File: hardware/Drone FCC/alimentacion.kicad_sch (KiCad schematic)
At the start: 1 part, among them J28 Conn_01x06

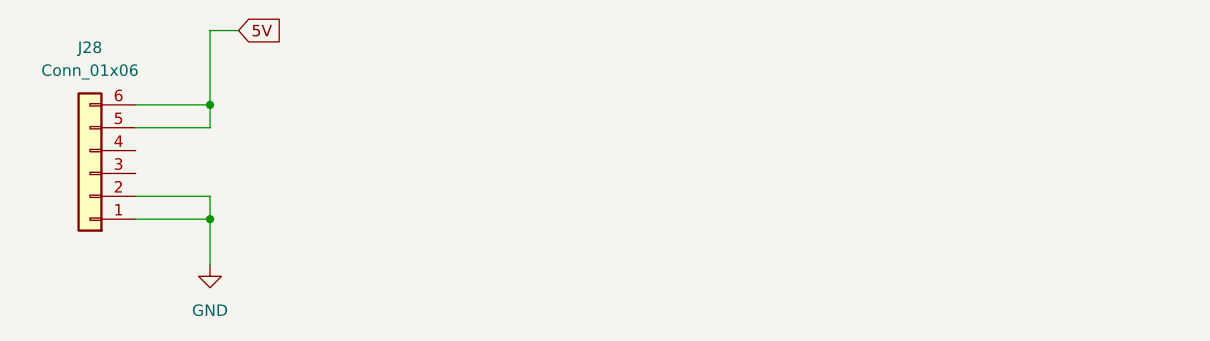
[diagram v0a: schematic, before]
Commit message: add LDO 3V3 to schematic
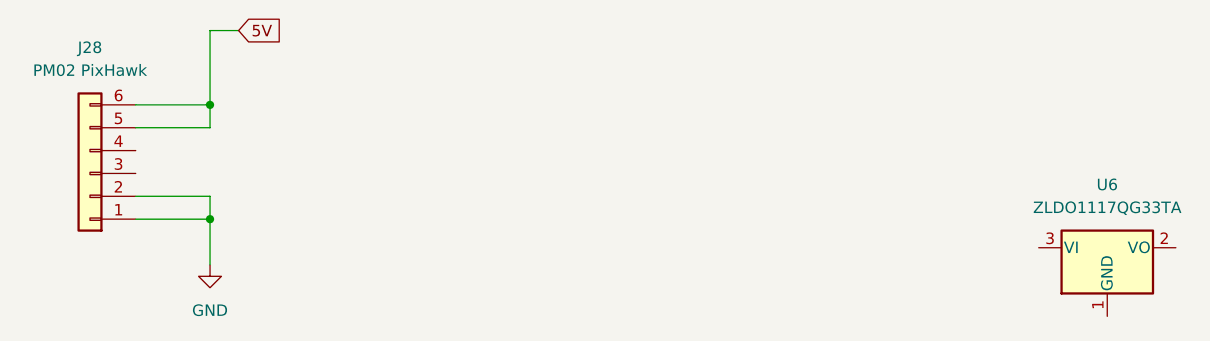
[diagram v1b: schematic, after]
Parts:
- added U6: ZLDO1117QG33TA, Package_TO_SOT_SMD:SOT-223-3_TabPin2, symbol Regulator_Linear:NCP1117-3.3_SOT223
- J28: value Conn_01x06 -> PM02 PixHawk
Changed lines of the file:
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@@
     (in_bom yes) (on_board yes) (fields_autoplaced)
     (property "Reference" "J28" (id 0) (at 41.275 35.56 0))
-    (property "Value" "Conn_01x06" (id 1) (at 41.275 38.1 0))
+    (property "Value" "PM02 PixHawk" (id 1) (at 41.275 38.1 0))
     (property "Footprint" "Connector_Hirose:Hirose_DF13C_CL535-0406-3-51_1x06-1MP_P1.25mm_Vertical" (id 2) (at 41.275 49.53 0)
       (effects (font (size 1.27 1.27)) hide)
@@
     (pin "6")
   )
+  (symbol (lib_id "Regulator_Linear:NCP1117-3.3_SOT223") (at 154.305 57.785 0) (unit 1)
+    (in_bom yes) (on_board yes) (fields_autoplaced)
+    (property "Reference" "U6" (id 0) (at 154.305 50.8 0))
+    (property "Value" "ZLDO1117QG33TA" (id 1) (at 154.305 53.34 0))
+    (property "Footprint" "Package_TO_SOT_SMD:SOT-223-3_TabPin2" (id 2) (at 154.305 52.705 0)
+      (effects (font (size 1.27 1.27)) hide)
+    )
+    (property "Datasheet" "http://www.onsemi.com/pub_link/Collateral/NCP1117-D.PDF" (id 3) (at 156.845 64.135 0)
+      (effects (font (size 1.27 1.27)) hide)
+    )
+    (pin "1")
+    (pin "2")
+    (pin "3")
+  )
   (symbol (lib_id "power:GND") (at 54.61 59.69 0) (unit 1)

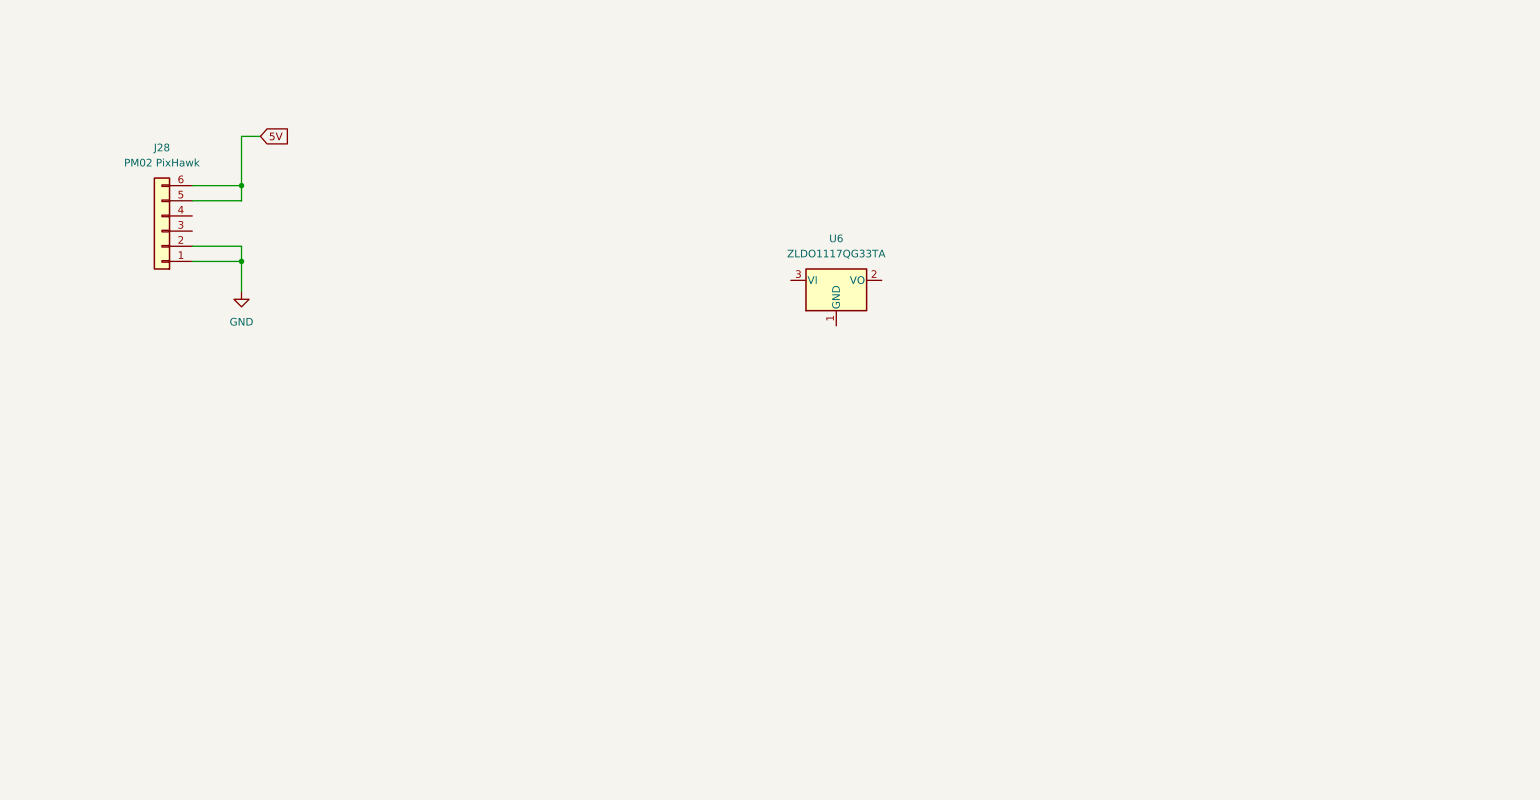
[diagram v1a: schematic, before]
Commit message: add soft-start for USB connector
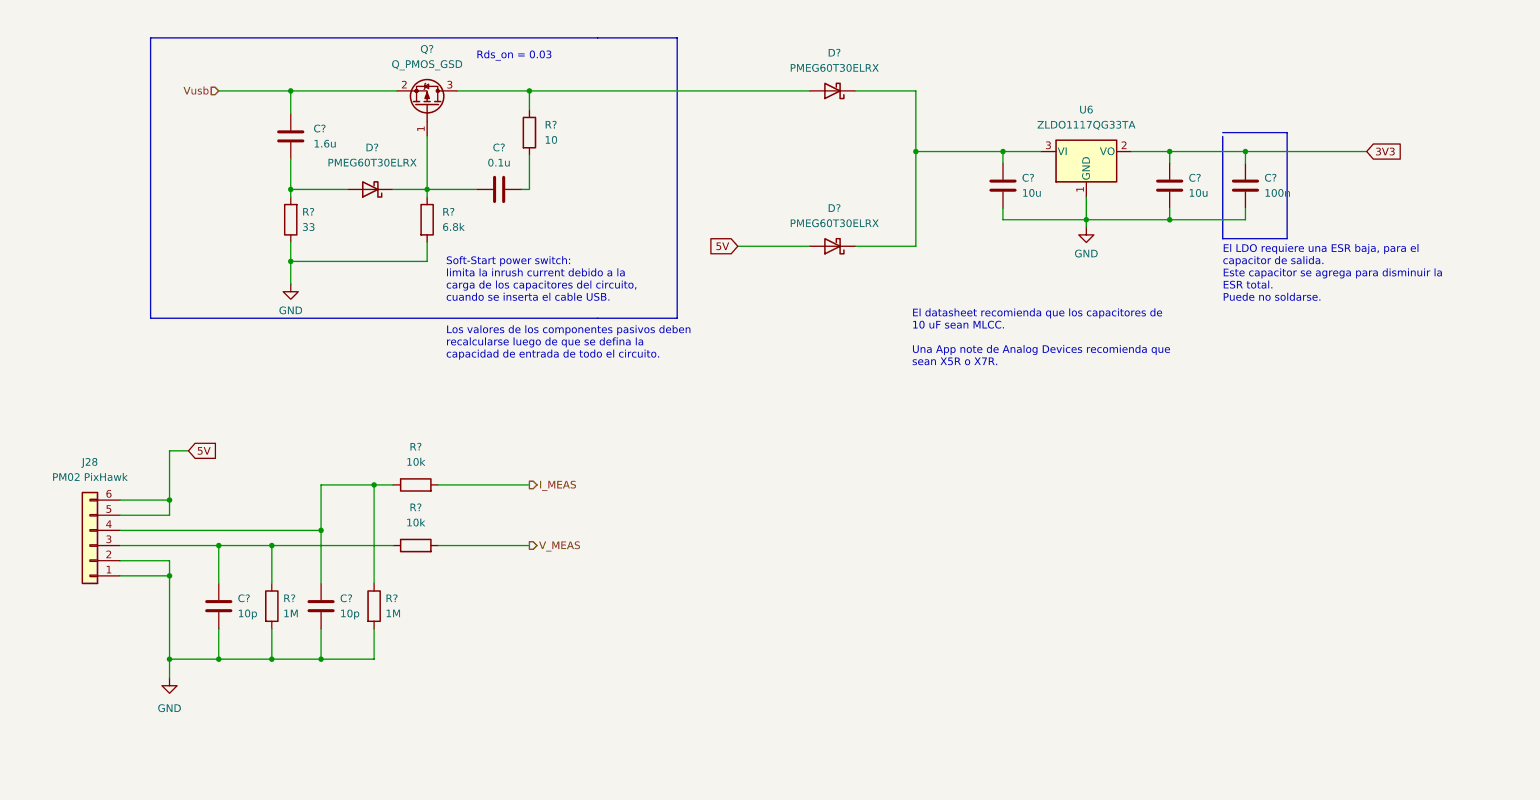
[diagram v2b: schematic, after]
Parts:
- added C?: 0.1u, symbol Device:C
- added C? (x2): 10u, symbol Device:C
- added C?: 1.6u, symbol Device:C
- added C? (x2): 10p, symbol Device:C
- added C?: 100n, symbol Device:C
- added D? (x3): PMEG60T30ELRX, symbol Device:D_Schottky
- added Q?: Q_PMOS_GSD, symbol Device:Q_PMOS_GSD
- added R?: 6.8k, symbol Device:R
- added R? (x2): 10k, symbol Device:R
- added R? (x2): 1M, symbol Device:R
- added R?: 10, symbol Device:R
- added R?: 33, symbol Device:R
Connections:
- net 5V: now also D?.2 (A)
- net GND: now also U6.1 (GND), C?.2, C?.2, C?.2, C?.2, C?.2, R?.1, R?.2, R?.2, R?.2
- net at J28.3 (Pin_3): now also C?.1, R?.1, R?.1
- net at J28.4 (Pin_4): now also C?.1, R?.1, R?.1
- net 3V3: now reaches U6.2 (VO)
- net 3V3: now also C?.1, C?.1
- net at U6.3 (VI): now also C?.1, D?.1 (K), D?.1 (K)
- new net: C?.1, D?.1 (K), Q?.1 (G), R?.1
- new net: C?.2, R?.2
- new net: D?.2 (A), Q?.3 (D), R?.1
- new net: C?.2, D?.2 (A), R?.2
- new net I_MEAS: R?.2
- new net V_MEAS: R?.2
- new net Vusb: C?.1, Q?.2 (S)
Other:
- note added: "El LDO requiere una ESR baja, para el capacitor de salida. Este capacitor se agrega para disminuir la ESR total. Puede no soldarse."
- note added: "El datasheet recomienda que los capacitores de 10 uF sean MLCC. Una App note de Analog Devices recomienda que sean X5R o X7R."
- note added: "Los valores de los componentes pasivos deben recalcularse luego de que se defina la capacidad de entrada de todo el circuito."
- note added: "Rds_on = 0.03"
- note added: "Soft-Start power switch: limita la inrush current debido a la carga de los capacitores del circuito, cuando se inserta el cable USB."
- moved on the sheet: J28, U6

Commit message: add CAN schematic
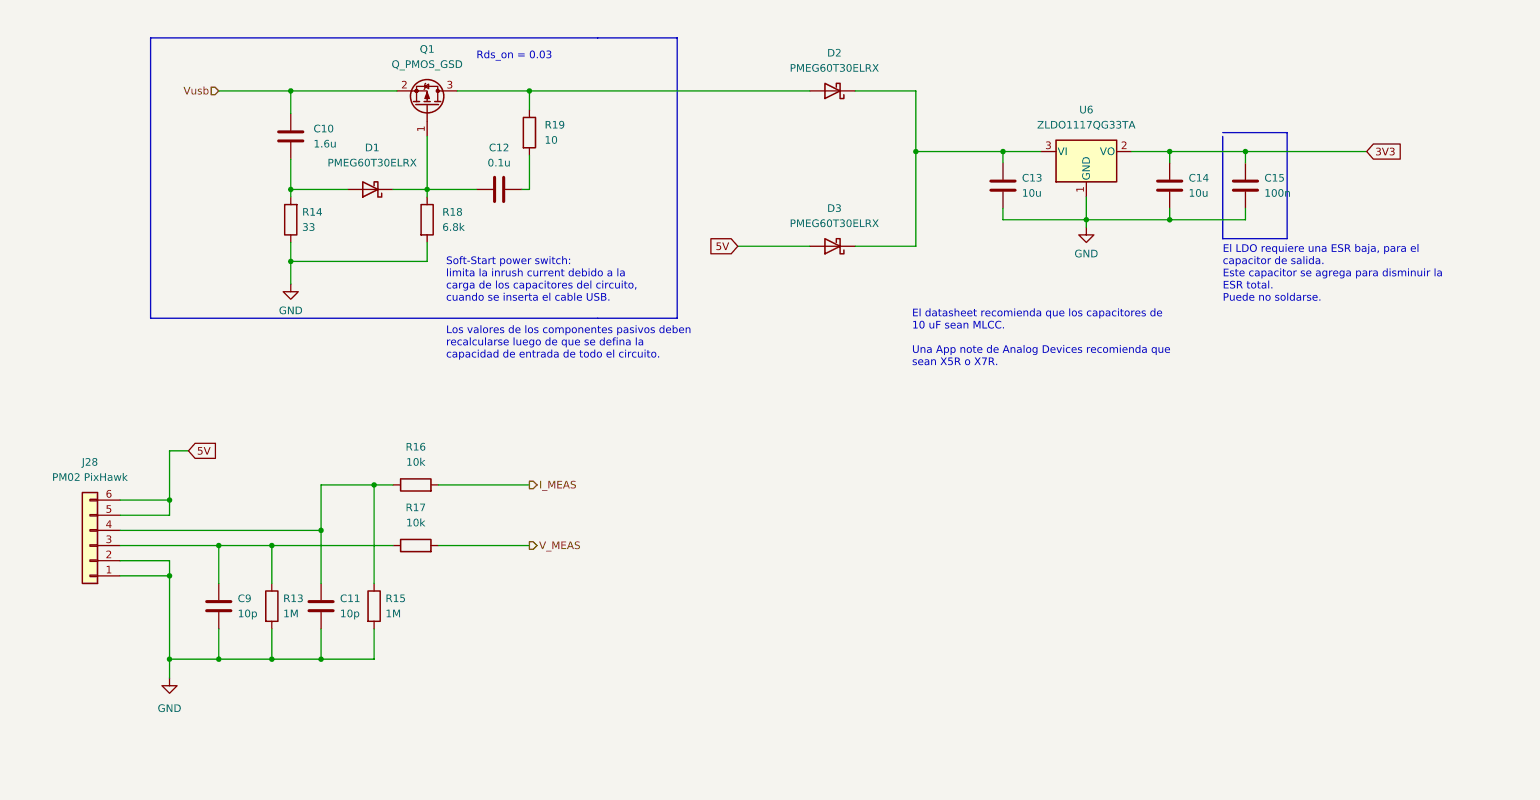
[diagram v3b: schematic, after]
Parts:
- gave numbers to parts that had none: 18
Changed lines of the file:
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@@
   (symbol (lib_id "Device:C") (at 97.79 42.545 90) (unit 1)
     (in_bom yes) (on_board yes) (fields_autoplaced)
-    (property "Reference" "C?" (id 0) (at 97.79 35.56 90))
+    (property "Reference" "C12" (id 0) (at 97.79 35.56 90))
     (property "Value" "0.1u" (id 1) (at 97.79 38.1 90))
     (property "Footprint" "" (id 2) (at 101.6 41.5798 0)
@@
   (symbol (lib_id "Device:Q_PMOS_GSD") (at 85.725 28.575 270) (mirror x) (unit 1)
     (in_bom yes) (on_board yes) (fields_autoplaced)
-    (property "Reference" "Q?" (id 0) (at 85.725 19.05 90))
+    (property "Reference" "Q1" (id 0) (at 85.725 19.05 90))
     (property "Value" "Q_PMOS_GSD" (id 1) (at 85.725 21.59 90))
     (property "Footprint" "" (id 2) (at 88.265 23.495 0)
@@
   (symbol (lib_id "Device:D_Schottky") (at 76.2 42.545 180) (unit 1)
     (in_bom yes) (on_board yes) (fields_autoplaced)
-    (property "Reference" "D?" (id 0) (at 76.5175 35.56 0))
+    (property "Reference" "D1" (id 0) (at 76.5175 35.56 0))
     (property "Value" "PMEG60T30ELRX " (id 1) (at 76.5175 38.1 0))
     (property "Footprint" "" (id 2) (at 76.2 42.545 0)
@@
   (symbol (lib_id "Device:R") (at 85.725 47.625 0) (unit 1)
     (in_bom yes) (on_board yes) (fields_autoplaced)
-    (property "Reference" "R?" (id 0) (at 88.265 46.3549 0)
+    (property "Reference" "R18" (id 0) (at 88.265 46.3549 0)
       (effects (font (size 1.27 1.27)) (justify left))
     )
@@
   (symbol (lib_id "Device:R") (at 83.82 102.235 90) (unit 1)
     (in_bom yes) (on_board yes) (fields_autoplaced)
-    (property "Reference" "R?" (id 0) (at 83.82 95.885 90))
+    (property "Reference" "R17" (id 0) (at 83.82 95.885 90))
     (property "Value" "10k" (id 1) (at 83.82 98.425 90))
     (property "Footprint" "" (id 2) (at 83.82 104.013 90)
@@
   (symbol (lib_id "power:GND") (at 62.865 58.42 0) (unit 1)
     (in_bom yes) (on_board yes) (fields_autoplaced)
-    (property "Reference" "#PWR?" (id 0) (at 62.865 64.77 0)
+    (property "Reference" "#PWR0128" (id 0) (at 62.865 64.77 0)
       (effects (font (size 1.27 1.27)) hide)
     )
@@
   (symbol (lib_id "Device:R") (at 76.835 112.395 0) (unit 1)
     (in_bom yes) (on_board yes) (fields_autoplaced)
-    (property "Reference" "R?" (id 0) (at 78.74 111.1249 0)
+    (property "Reference" "R15" (id 0) (at 78.74 111.1249 0)
       (effects (font (size 1.27 1.27)) (justify left))
     )
@@
   (symbol (lib_id "Device:C") (at 182.245 41.91 0) (unit 1)
     (in_bom yes) (on_board yes) (fields_autoplaced)
-    (property "Reference" "C?" (id 0) (at 185.42 40.6399 0)
+    (property "Reference" "C13" (id 0) (at 185.42 40.6399 0)
       (effects (font (size 1.27 1.27)) (justify left))
     )
@@
   (symbol (lib_id "Device:R") (at 59.69 112.395 0) (unit 1)
     (in_bom yes) (on_board yes) (fields_autoplaced)
-    (property "Reference" "R?" (id 0) (at 61.595 111.1249 0)
+    (property "Reference" "R13" (id 0) (at 61.595 111.1249 0)
       (effects (font (size 1.27 1.27)) (justify left))
     )
@@
   (symbol (lib_id "Device:C") (at 62.865 33.655 0) (unit 1)
     (in_bom yes) (on_board yes) (fields_autoplaced)
-    (property "Reference" "C?" (id 0) (at 66.675 32.3849 0)
+    (property "Reference" "C10" (id 0) (at 66.675 32.3849 0)
       (effects (font (size 1.27 1.27)) (justify left))
     )
@@
   (symbol (lib_id "Device:R") (at 102.87 33.02 0) (unit 1)
     (in_bom yes) (on_board yes) (fields_autoplaced)
-    (property "Reference" "R?" (id 0) (at 105.41 31.7499 0)
+    (property "Reference" "R19" (id 0) (at 105.41 31.7499 0)
       (effects (font (size 1.27 1.27)) (justify left))
     )
@@
   (symbol (lib_id "Device:C") (at 50.8 112.395 0) (unit 1)
     (in_bom yes) (on_board yes) (fields_autoplaced)
-    (property "Reference" "C?" (id 0) (at 53.975 111.1249 0)
+    (property "Reference" "C9" (id 0) (at 53.975 111.1249 0)
       (effects (font (size 1.27 1.27)) (justify left))
     )
@@
   (symbol (lib_id "Device:R") (at 62.865 47.625 180) (unit 1)
     (in_bom yes) (on_board yes) (fields_autoplaced)
-    (property "Reference" "R?" (id 0) (at 64.77 46.3549 0)
+    (property "Reference" "R14" (id 0) (at 64.77 46.3549 0)
       (effects (font (size 1.27 1.27)) (justify right))
     )
@@
   (symbol (lib_id "Device:D_Schottky") (at 153.67 26.035 180) (unit 1)
     (in_bom yes) (on_board yes) (fields_autoplaced)
-    (property "Reference" "D?" (id 0) (at 153.9875 19.685 0))
+    (property "Reference" "D2" (id 0) (at 153.9875 19.685 0))
     (property "Value" "PMEG60T30ELRX " (id 1) (at 153.9875 22.225 0))
     (property "Footprint" "" (id 2) (at 153.67 26.035 0)
@@
   (symbol (lib_id "Device:C") (at 222.885 41.91 0) (unit 1)
     (in_bom yes) (on_board yes) (fields_autoplaced)
-    (property "Reference" "C?" (id 0) (at 226.06 40.6399 0)
+    (property "Reference" "C15" (id 0) (at 226.06 40.6399 0)
       (effects (font (size 1.27 1.27)) (justify left))
     )
@@
   (symbol (lib_id "Device:R") (at 83.82 92.075 90) (unit 1)
     (in_bom yes) (on_board yes) (fields_autoplaced)
-    (property "Reference" "R?" (id 0) (at 83.82 85.725 90))
+    (property "Reference" "R16" (id 0) (at 83.82 85.725 90))
     (property "Value" "10k" (id 1) (at 83.82 88.265 90))
     (property "Footprint" "" (id 2) (at 83.82 93.853 90)
@@
   (symbol (lib_id "Device:C") (at 210.185 41.91 0) (unit 1)
     (in_bom yes) (on_board yes) (fields_autoplaced)
-    (property "Reference" "C?" (id 0) (at 213.36 40.6399 0)
+    (property "Reference" "C14" (id 0) (at 213.36 40.6399 0)
       (effects (font (size 1.27 1.27)) (justify left))
     )
@@
   (symbol (lib_id "Device:C") (at 67.945 112.395 0) (unit 1)
     (in_bom yes) (on_board yes) (fields_autoplaced)
-    (property "Reference" "C?" (id 0) (at 71.12 111.1249 0)
+    (property "Reference" "C11" (id 0) (at 71.12 111.1249 0)
       (effects (font (size 1.27 1.27)) (justify left))
     )
@@
   (symbol (lib_id "power:GND") (at 196.215 48.895 0) (unit 1)
     (in_bom yes) (on_board yes) (fields_autoplaced)
-    (property "Reference" "#PWR?" (id 0) (at 196.215 55.245 0)
+    (property "Reference" "#PWR0129" (id 0) (at 196.215 55.245 0)
       (effects (font (size 1.27 1.27)) hide)
     )
@@
   (symbol (lib_id "Device:D_Schottky") (at 153.67 52.07 180) (unit 1)
     (in_bom yes) (on_board yes) (fields_autoplaced)
-    (property "Reference" "D?" (id 0) (at 153.9875 45.72 0))
+    (property "Reference" "D3" (id 0) (at 153.9875 45.72 0))
     (property "Value" "PMEG60T30ELRX " (id 1) (at 153.9875 48.26 0))
     (property "Footprint" "" (id 2) (at 153.67 52.07 0)

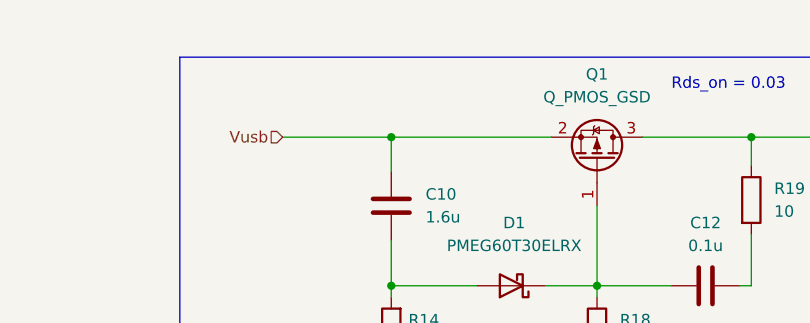
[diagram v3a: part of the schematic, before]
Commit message: rearranged FCC schematic
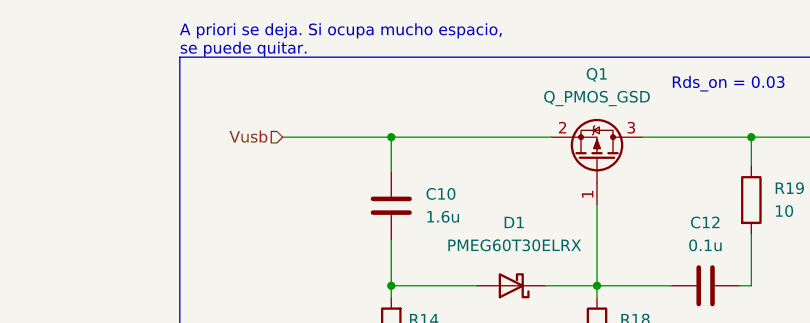
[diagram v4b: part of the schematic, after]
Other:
- note added: "A priori se deja. Si ocupa mucho espacio, se puede quitar."
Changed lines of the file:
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@@
+    (effects (font (size 1.27 1.27)) (justify left bottom))
+  )
+  (text "A priori se deja. Si ocupa mucho espacio,\nse puede quitar."
+    (at 39.37 17.145 0)
     (effects (font (size 1.27 1.27)) (justify left bottom))
   )
